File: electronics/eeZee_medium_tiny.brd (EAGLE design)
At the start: 28.7 x 16.3 mm, 11 parts, among them IC1 TINY24/44/84, J2 avrisp, Q1 16MHz

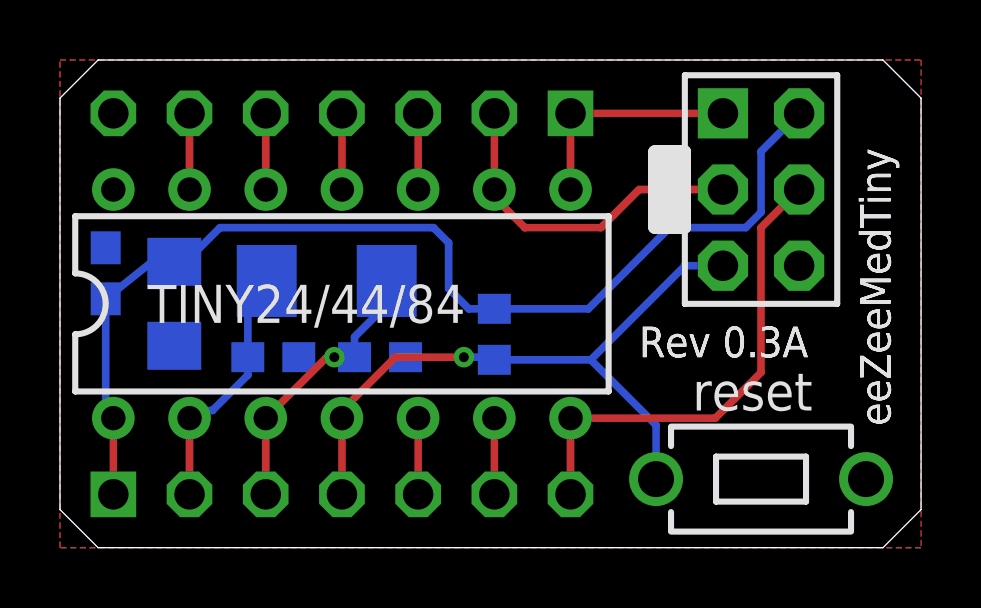
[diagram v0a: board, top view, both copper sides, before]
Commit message: update logo, silk, add help url
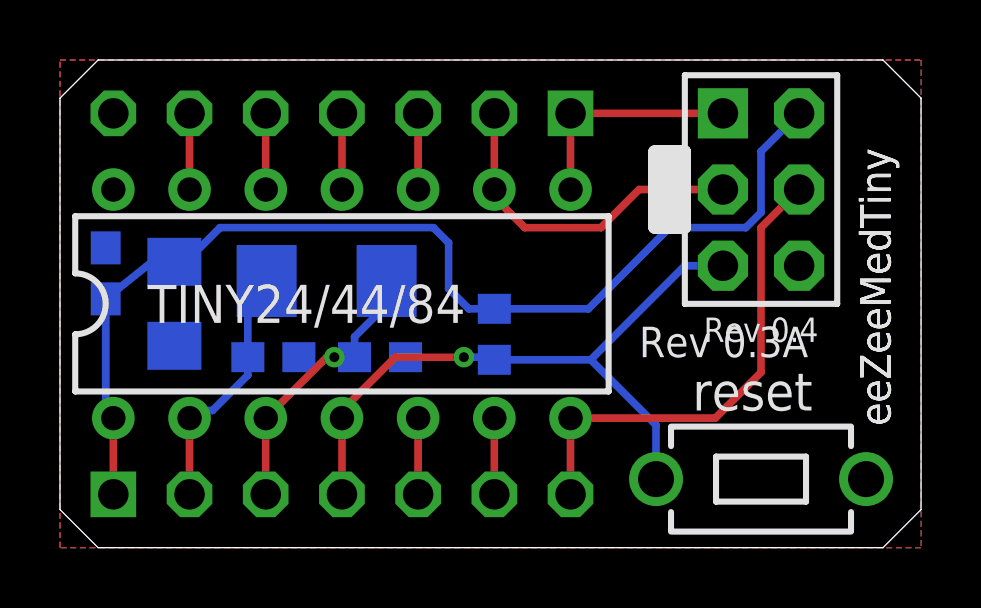
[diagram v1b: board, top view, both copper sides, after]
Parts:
- added U$1: BTLOGO-LOGO-SM, bt:BTLOGOS
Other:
- board text added: "Rev 0.4"
- board text added: "cc-by-sa"
- board text added: "is.gd/BC8POr"
